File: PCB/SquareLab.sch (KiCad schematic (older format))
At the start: 6 parts

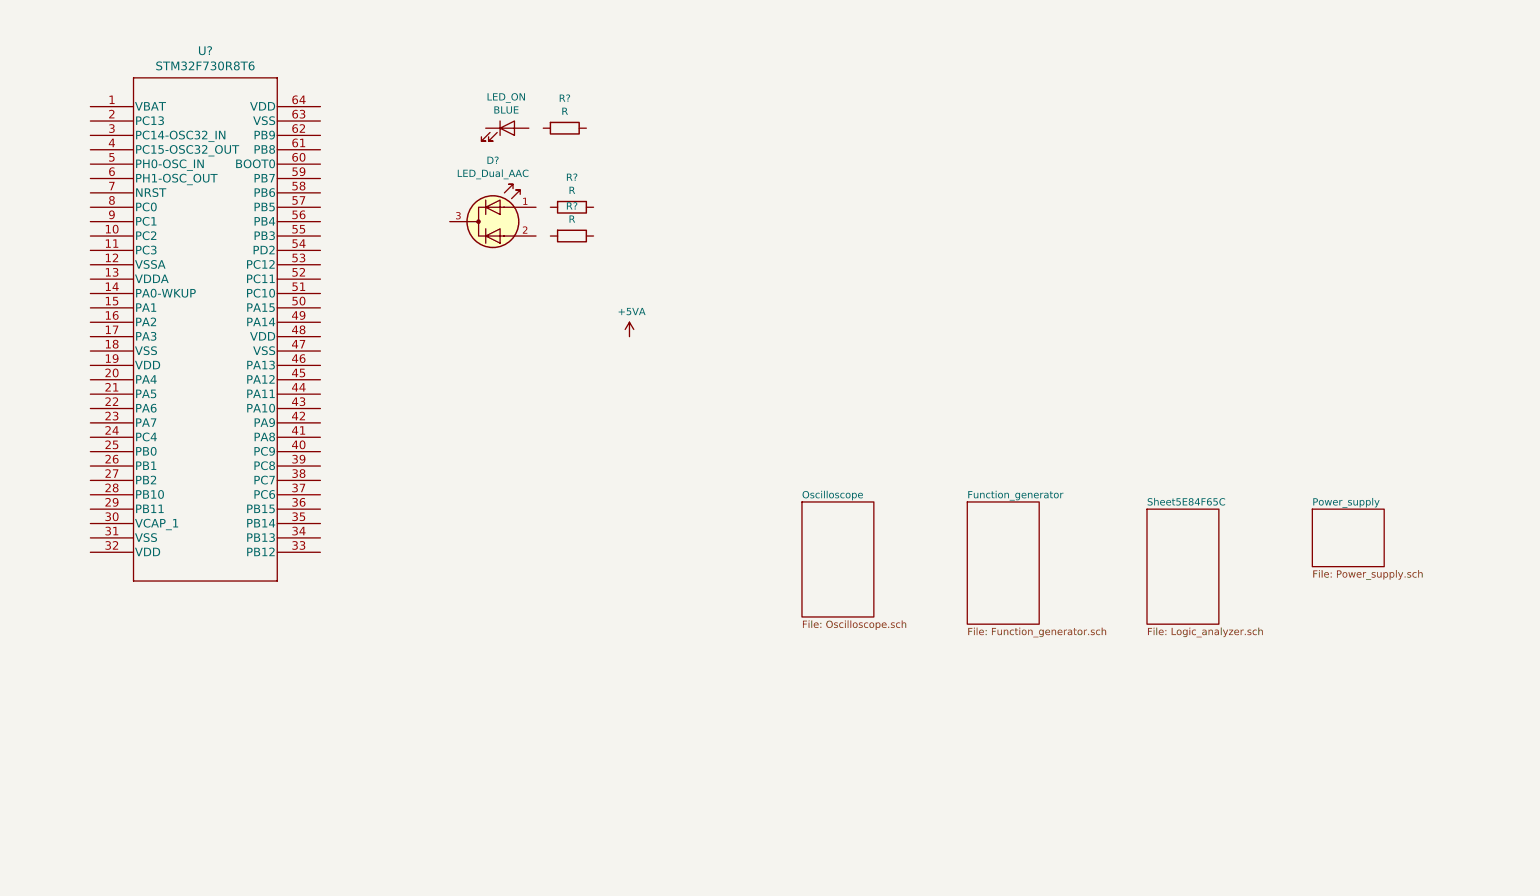
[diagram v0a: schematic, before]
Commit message: Added USB footprint and modified schematic
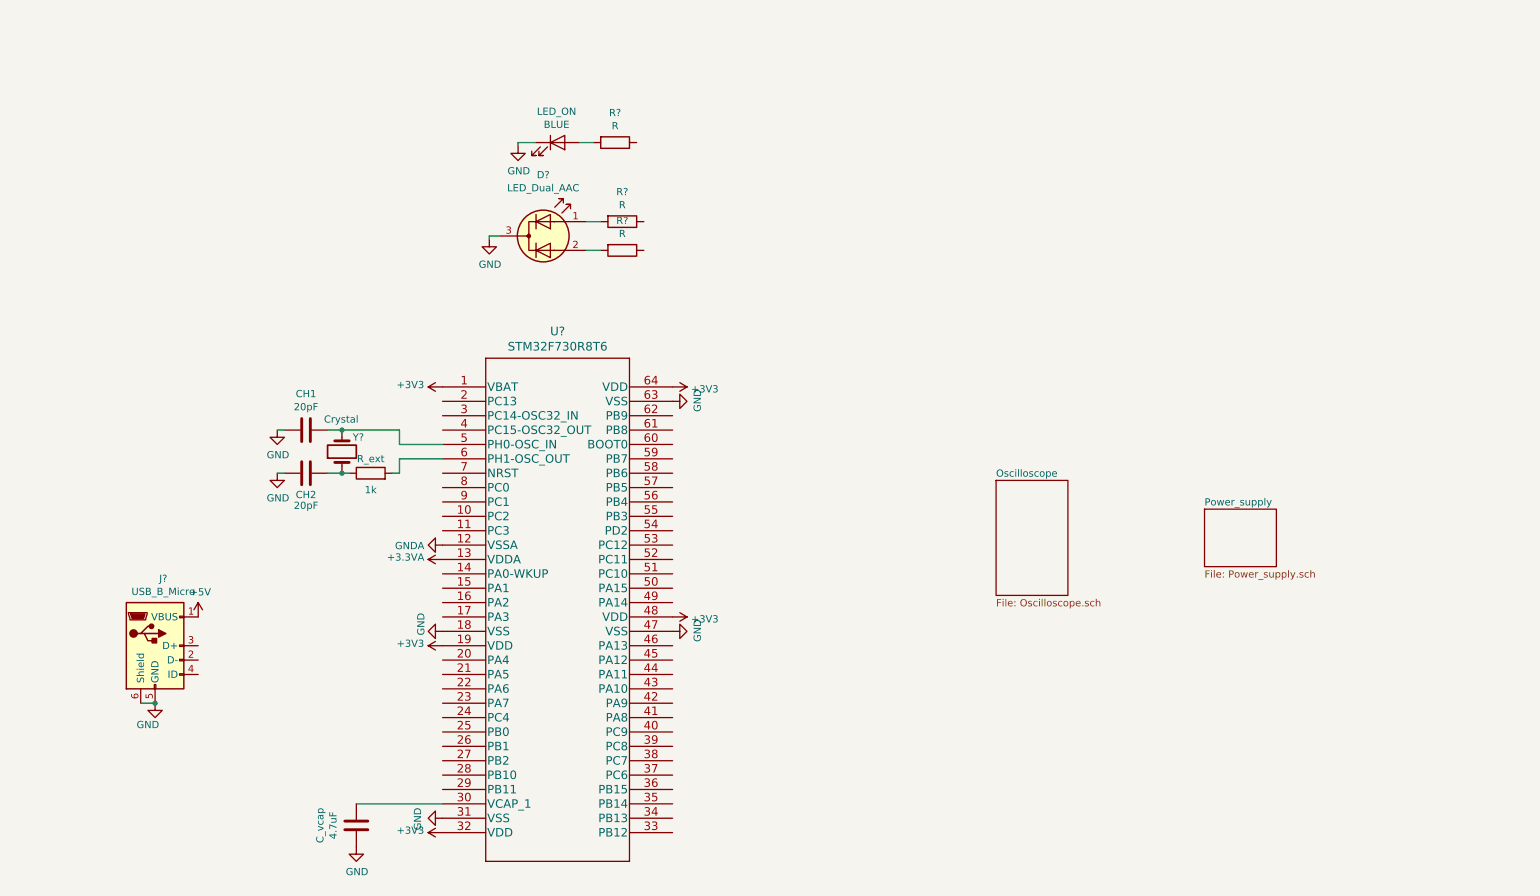
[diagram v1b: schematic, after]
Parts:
- added CH1, CH2: 20pF, symbol Device:C
- added C_vcap: 4.7uF, symbol Device:C
- added J?: USB_B_Micro, Amphenol_micro_usb:Amphenol_micro_USB, symbol Connector:USB_B_Micro
- added R_ext: 1k, symbol Device:R
- added Y?: Crystal, Crystal:Crystal_SMD_SeikoEpson_TSX3225-4Pin_3.2x2.5mm_HandSoldering, symbol Device:Crystal
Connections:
- net +3V3: now reaches U?.1 (VBAT)
- net +3V3: now also U?.19 (VDD), U?.32 (VDD), U?.48 (VDD), U?.64 (VDD)
- net GNDA: now reaches U?.12 (VSSA)
- net +3.3VA: now reaches U?.13 (VDDA)
- net GND: now reaches U?.18 (VSS)
- net GND: now also D?.3 (K), LED_ON.1 (K), U?.31 (VSS), U?.47 (VSS), U?.63 (VSS), CH1.2, CH2.2, C_vcap.2, J?.5 (GND), J?.6 (Shield)
- net at U?.30 (VCAP_1): now also C_vcap.1
- net at U?.5 (PH0-OSC_IN): now also CH1.1, Y?.2
- net at U?.6 (PH1-OSC_OUT): now also R_ext.2
- net at LED_ON.2 (A): now also R?.2
- net at D?.1 (A1): now also R?.2
- net at D?.2 (A2): now also R?.2
- new net: CH2.1, R_ext.1, Y?.1
- new net +5V: J?.1 (VBUS)
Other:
- moved on the sheet: D?, LED_ON, R?, U?

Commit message: Some updates schematic side
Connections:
- net DAC_OUT_1: now reaches U?.20 (PA4)
- net DAC_OUT_2: now reaches U?.21 (PA5)
- net OTG_HS_ID: now reaches U?.33 (PB12)
- net USB_HS_DM: now reaches U?.35 (PB14)
- net USB_HS_DM: now also J?.2 (D-)
- net USB_HS_DP: now reaches U?.36 (PB15)
- net USB_HS_DP: now also J?.3 (D+)
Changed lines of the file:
@@
 	1450 5400 1550 5400
 Connection ~ 1550 5400
+Text GLabel 3550 5100 0    50   Input ~ 0
+DAC_OUT_1
+Text GLabel 3550 5200 0    50   Input ~ 0
+DAC_OUT_2
+Text GLabel 5150 6000 2    50   Input ~ 0
+USB_HS_DP
+Text GLabel 5150 6100 2    50   Input ~ 0
+USB_HS_DM
+Text GLabel 1850 5000 2    50   Input ~ 0
+USB_HS_DP
+Text GLabel 1850 5100 2    50   Input ~ 0
+USB_HS_DM
+Text GLabel 5150 6300 2    50   Input ~ 0
+OTG_HS_ID
 $EndSCHEMATC

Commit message: Advancing in the schmatic. Power to be finished
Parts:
- added C? (x6): C, symbol Device:C
- added R_ext? (x2): 10k, symbol Device:R
- added SW?: Reset, symbol Switch:SW_Push
- added SW?: Boot, symbol Switch:SW_Push
- R? (x3): value R -> 330R
- Y?: value Crystal -> 16MHz
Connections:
- net labels added: D1, D10, D11, D12, D13, D14, D15, D16, D17, D18, D19, D2, D20, D21, D22, D23, D24, D3, D4, D5, D6, D7, D8, D9, dac_out_1, dac_out_2, led_heartbeat, led_usb_state, oscilloscope_channel_1, oscilloscope_channel_2, oscilloscope_channel_3, oscilloscope_channel_4, trig_out_1, trig_out_2, trig_out_3, trig_out_4
- net labels removed: DAC_OUT_1, DAC_OUT_2
- wire segments 20 -> 88
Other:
- moved on the sheet: CH1, CH2, C_vcap, D?, J?, LED_ON, R?, R_ext, U?, Y?

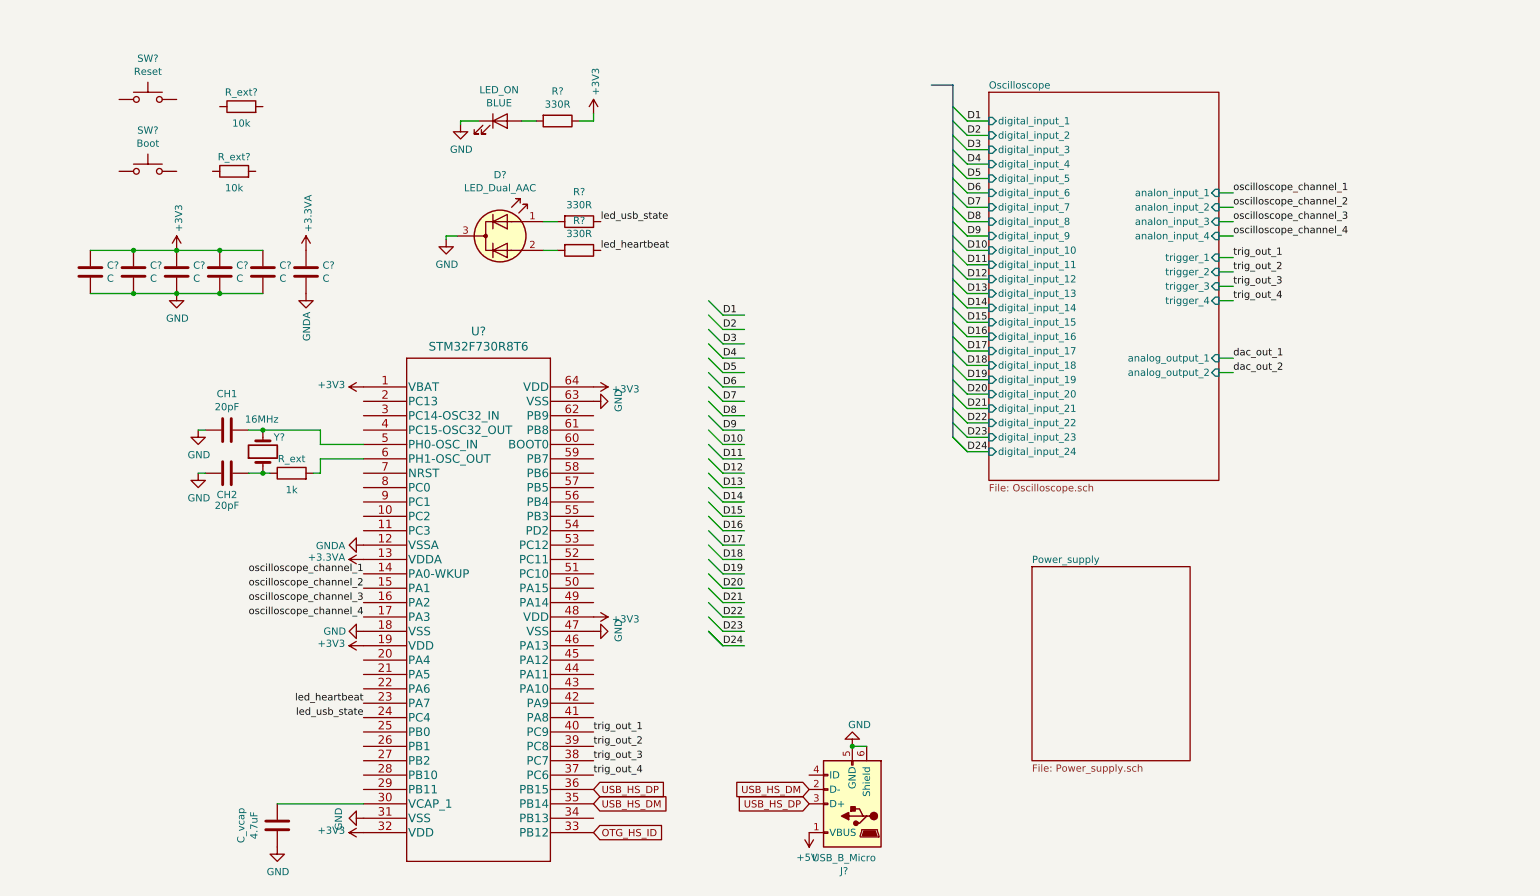
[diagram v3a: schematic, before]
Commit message: Changed microcontroller, schemtic modified
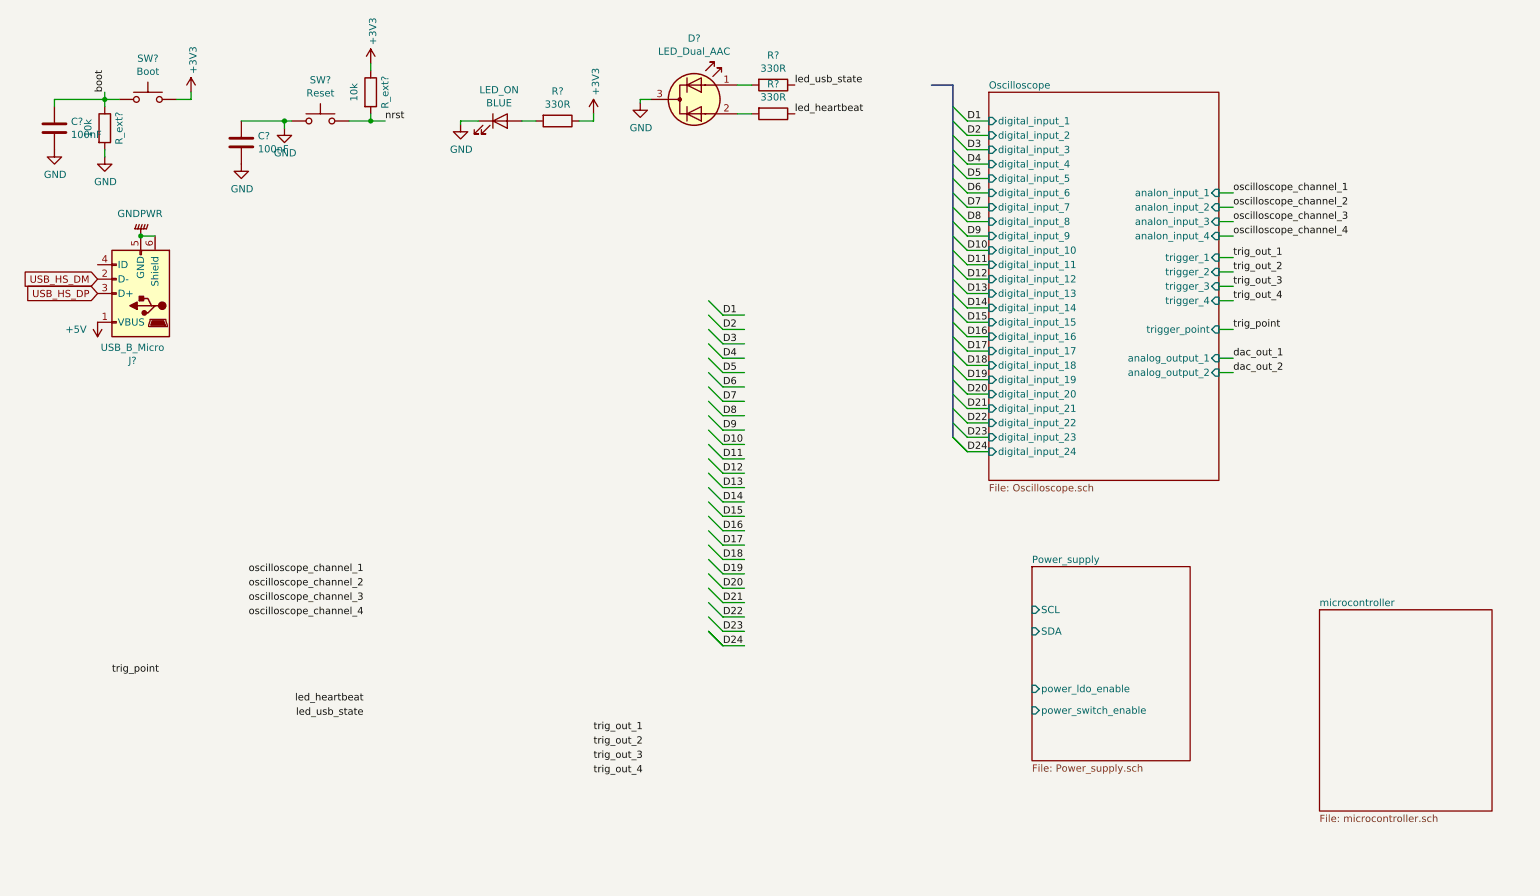
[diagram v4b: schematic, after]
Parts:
- removed C? (x6): C, symbol Device:C
- removed CH1, CH2: 20pF, symbol Device:C
- removed C_vcap: 4.7uF, symbol Device:C
- removed R_ext: 1k, symbol Device:R
- removed U?: STM32F730R8T6, QFP_730R8T6_STM, symbol STM32_UL:STM32F730R8T6
- removed Y?: 16MHz, Crystal:Crystal_SMD_SeikoEpson_TSX3225-4Pin_3.2x2.5mm_HandSoldering, symbol Device:Crystal
- added C? (x2): 100nF, symbol Device:C
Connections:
- net labels added: GNDPWR, boot, nrst, trig_point
- net labels removed: +3.3VA, GNDA, OTG_HS_ID
- wire segments 88 -> 84
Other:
- moved on the sheet: D?, J?, R?, R_ext?, SW?

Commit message: Advancement in schematic regarding oscilloscope and power supply
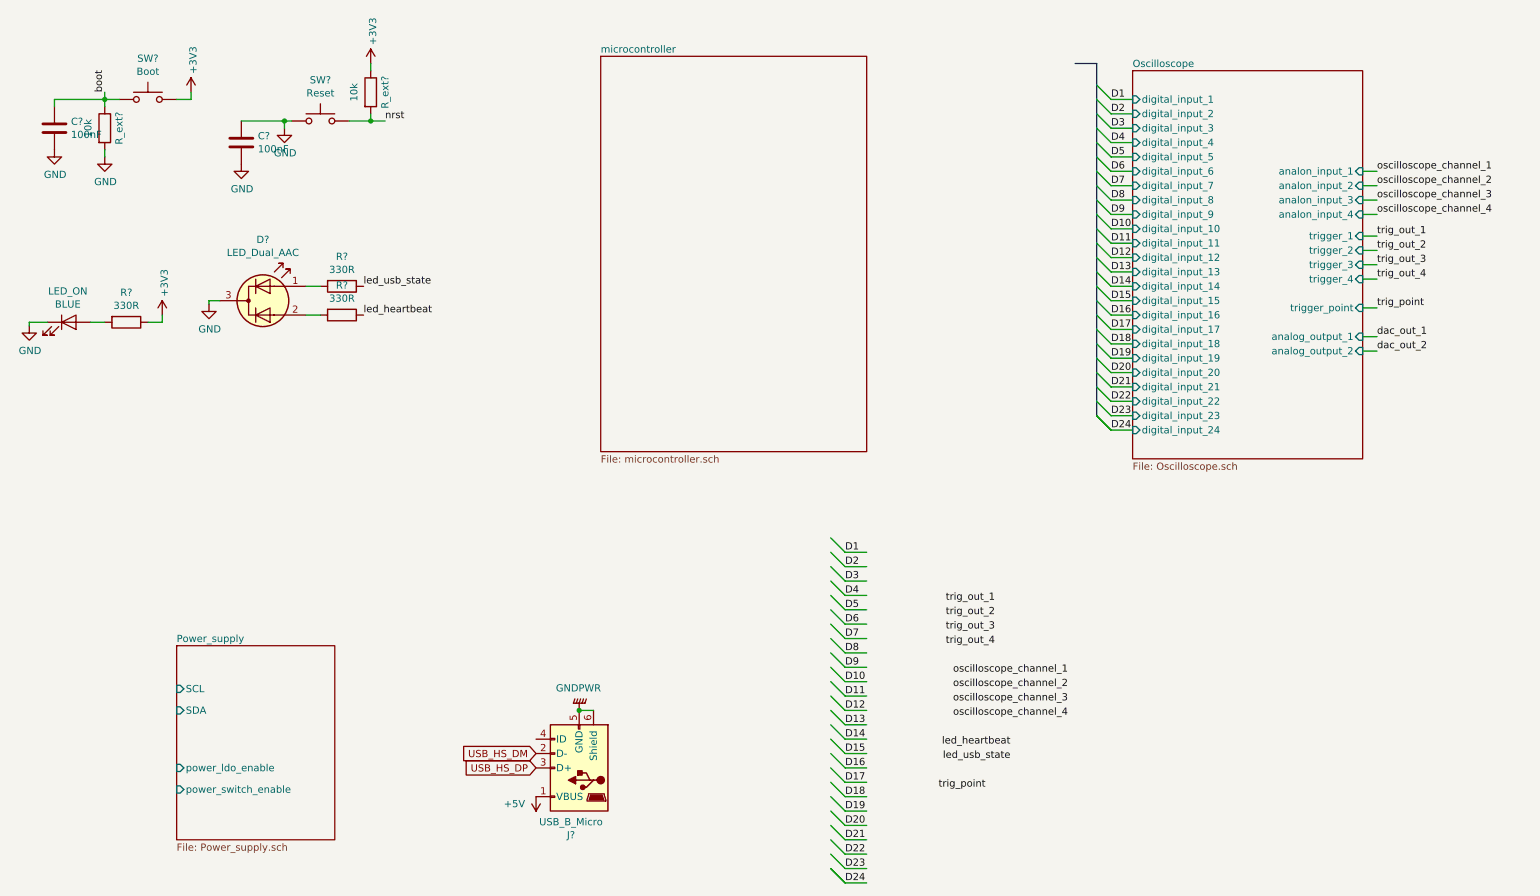
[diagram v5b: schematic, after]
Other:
- moved on the sheet: D?, J?, LED_ON, R?
